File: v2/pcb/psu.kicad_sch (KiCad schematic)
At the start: 44 parts, among them J1 USB_C_Receptacle_USB2.0, J3 U.FL, J4 U.FL, J5 U.FL, U1 STM32H750XBH6, U12 ZLDO1117-33

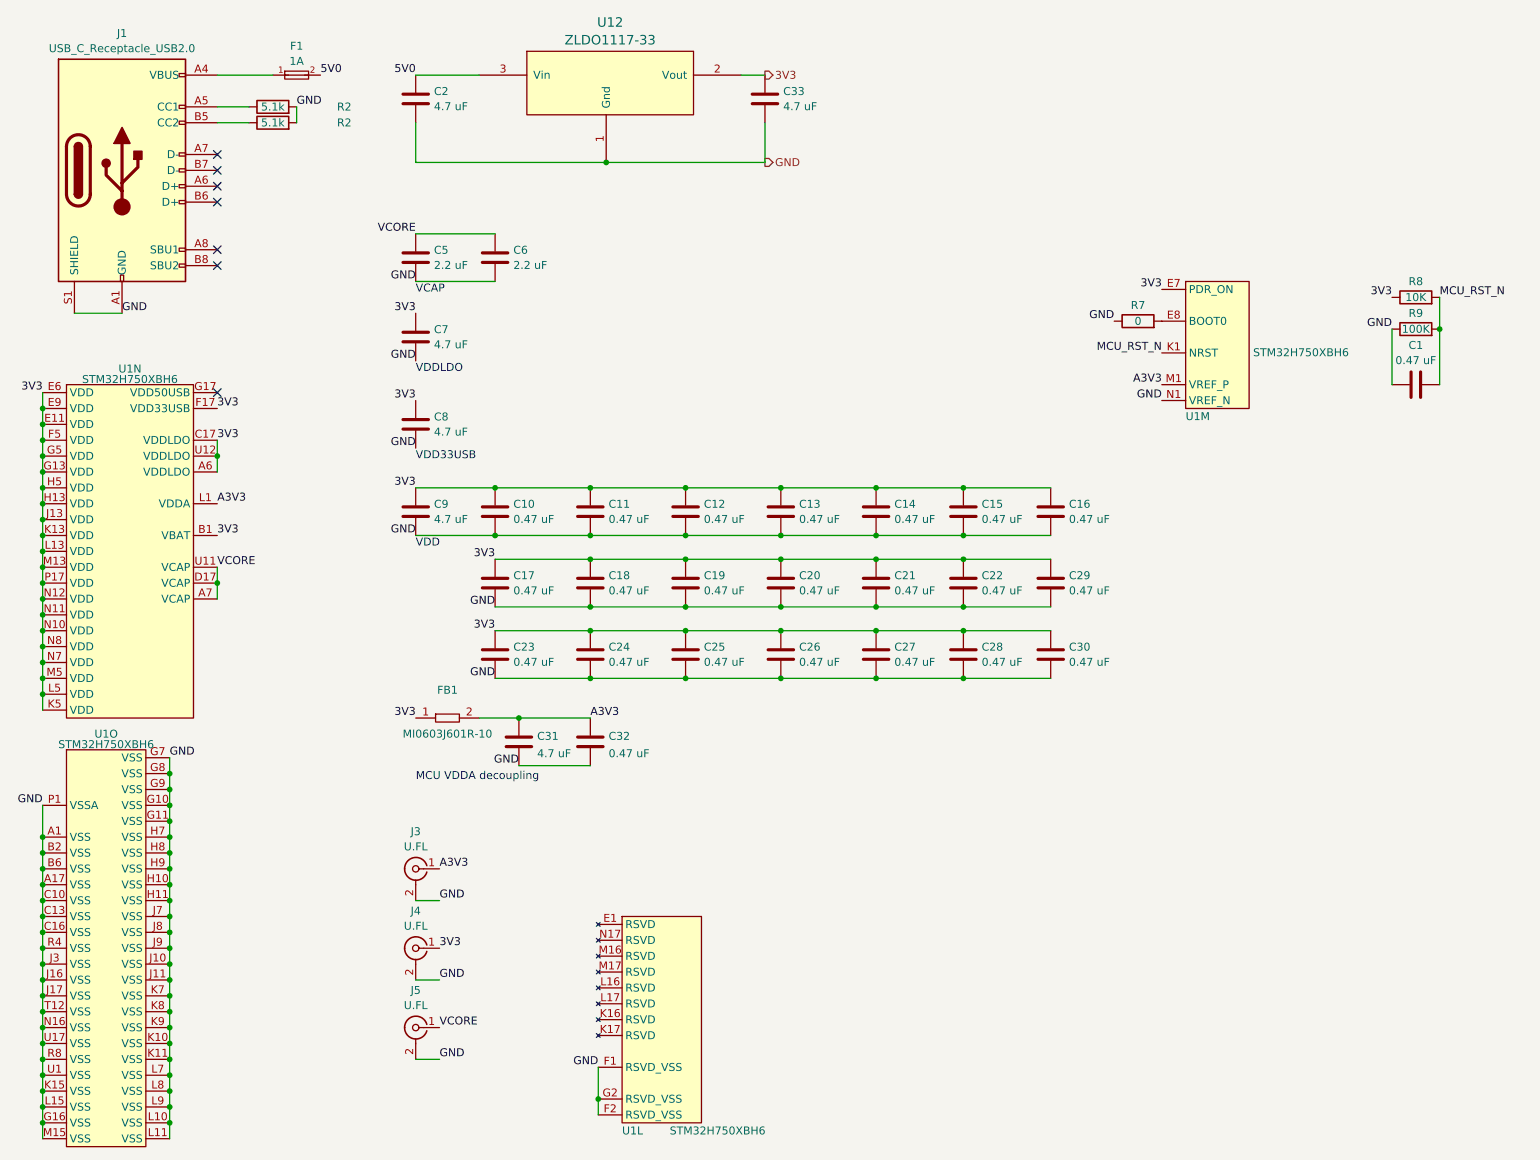
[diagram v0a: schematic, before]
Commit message: Finished initial MCU layout, need to actually add challenges
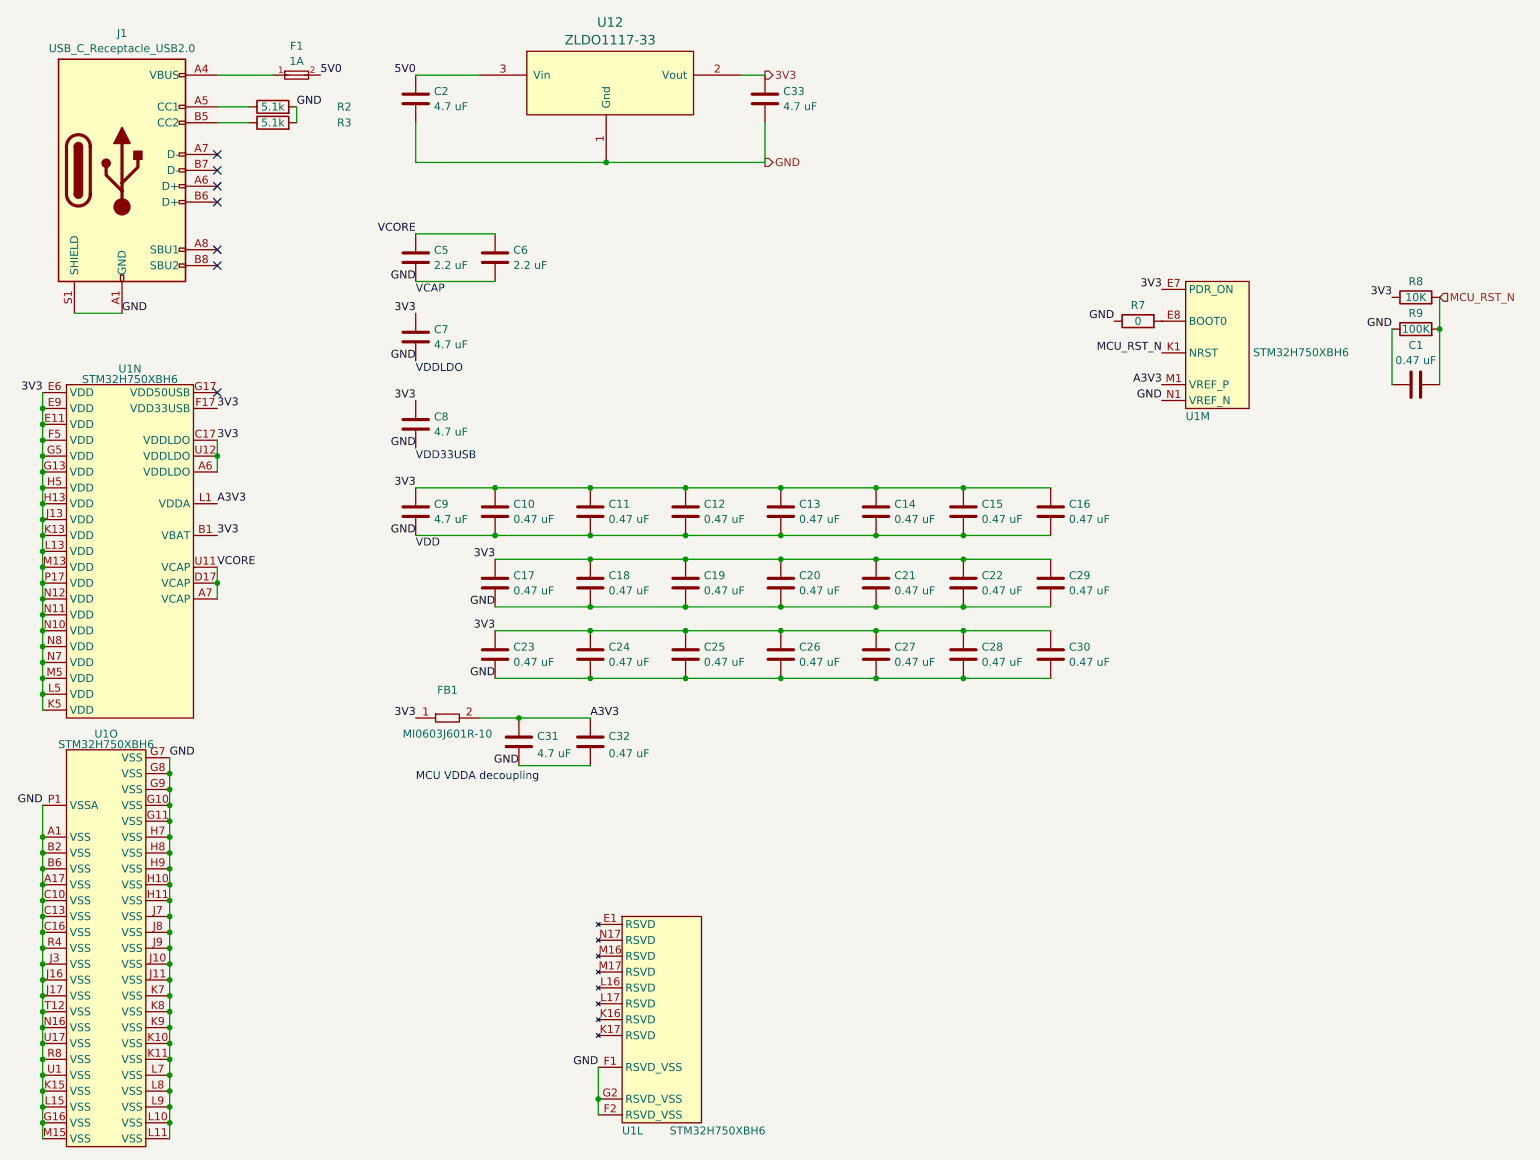
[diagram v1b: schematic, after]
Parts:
- removed J3, J4, J5: U.FL, azonenberg_pcb:CONN_U.FL_TE_1909763-1, symbol conn:CONN_COAXIAL
- renumbered R2 to R3

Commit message: Got up to challenge 8
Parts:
- J1: footprint Connector_USB:USB_C_Receptacle_HRO_TYPE-C-31-M-12 -> lain:GCT_USB4500-03-0-A
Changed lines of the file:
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@@
 			)
 		)
-		(property "Footprint" "Connector_USB:USB_C_Receptacle_HRO_TYPE-C-31-M-12"
+		(property "Footprint" "lain:GCT_USB4500-03-0-A"
 			(at 36.83 39.37 0)
 			(effects
